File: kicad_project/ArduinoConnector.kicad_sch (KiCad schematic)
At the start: 12 parts, among them J5 1x8, J6 1x6, J7 1x10, J8 1x8

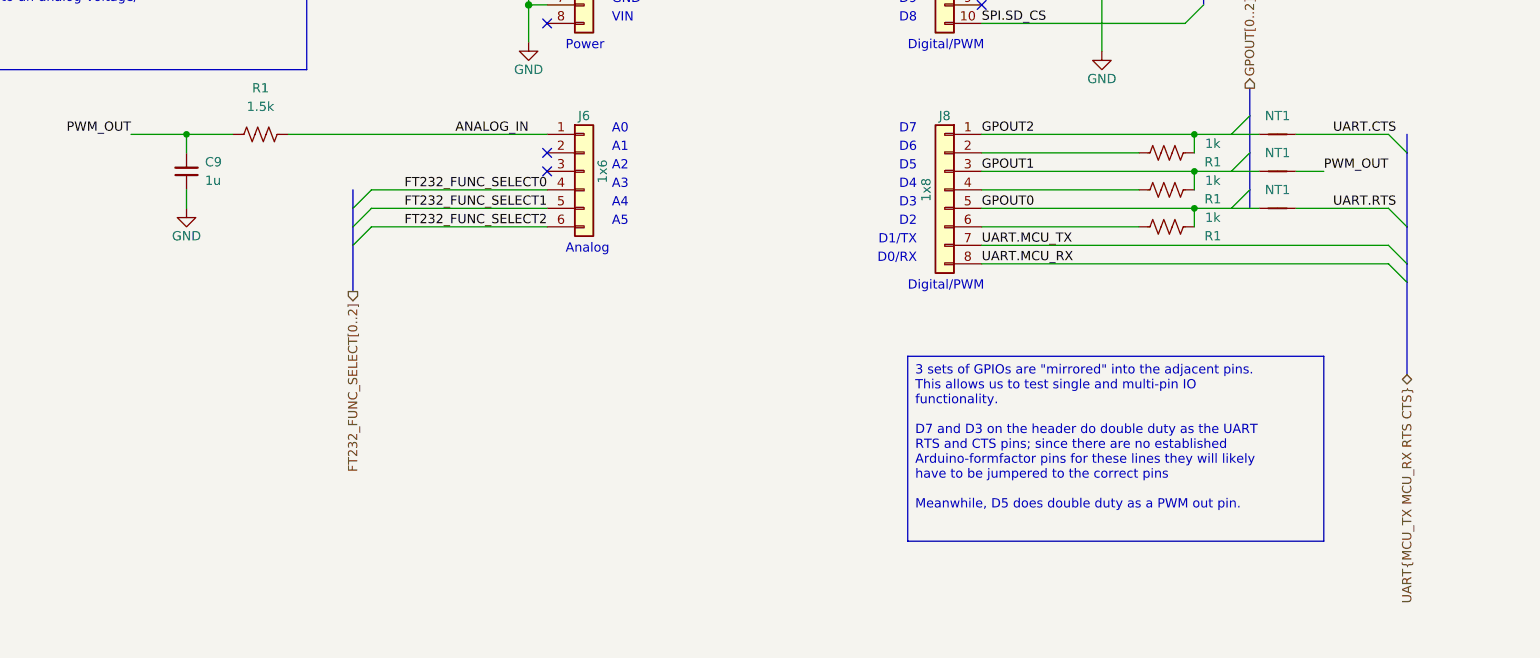
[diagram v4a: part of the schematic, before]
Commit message: Add diode on SD card CS line, fix position of PWM/analog testing capacitor
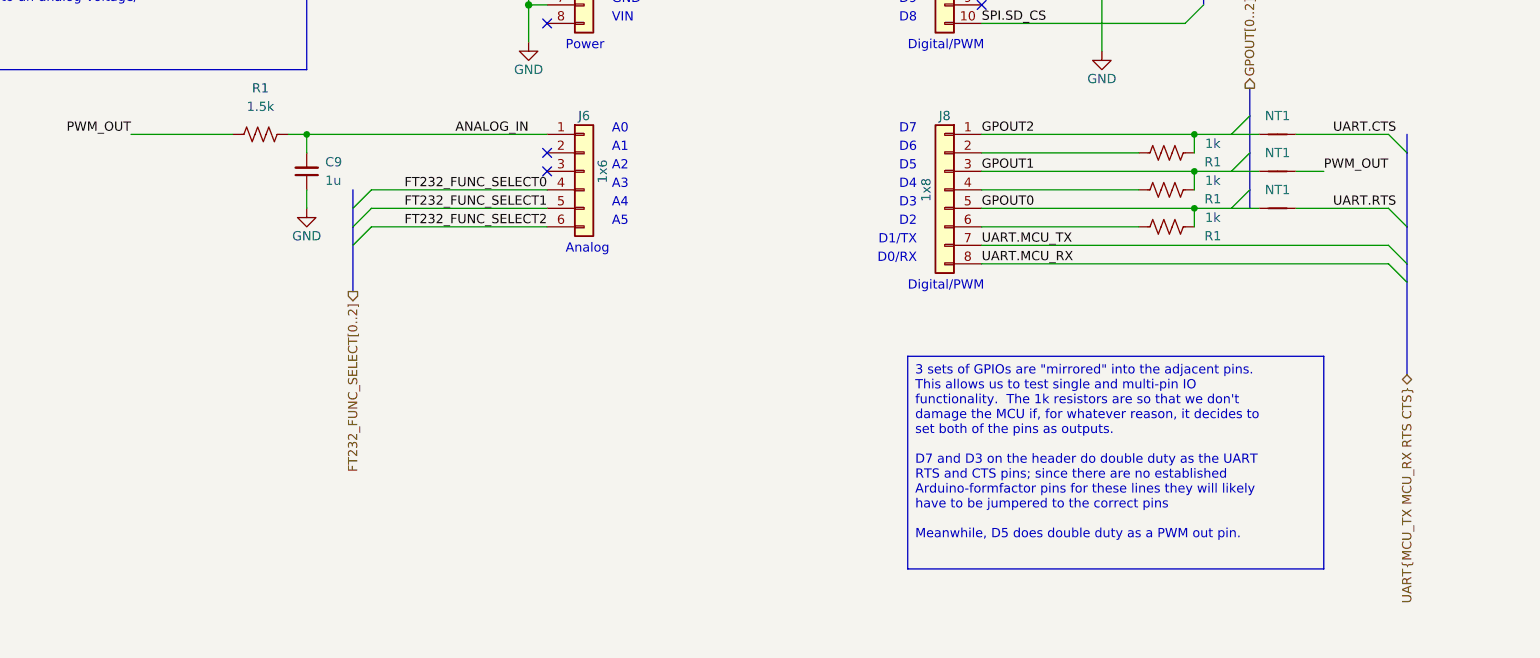
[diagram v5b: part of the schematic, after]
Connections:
- net ANALOG_IN: now also C9.2
- net PWM_OUT: no longer C9.2
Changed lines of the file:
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@@
   (junction (at 210.82 107.95) (diameter 0) (color 0 0 0 0)
   )
-  (junction (at 72.39 97.79) (diameter 0) (color 0 0 0 0)
-  )
   (junction (at 210.82 97.79) (diameter 0) (color 0 0 0 0)
+  )
+  (junction (at 88.9 97.79) (diameter 0) (color 0 0 0 0)
   )
   (junction (at 119.38 80.01) (diameter 1.016) (color 0 0 0 0)
@@
     (stroke (width 0) (type default))
   )
-  (wire (pts (xy 72.39 97.79) (xy 72.39 100.33))
-    (stroke (width 0) (type default))
-  )
   (bus (pts (xy 240.03 118.11) (xy 240.03 130.81))
     (stroke (width 0) (type default))
@@
     (stroke (width 0) (type default))
   )
+  (wire (pts (xy 88.9 105.41) (xy 88.9 107.95))
+    (stroke (width 0) (type default))
+  )
   (bus (pts (xy 95.25 105.41) (xy 95.25 107.95))
     (stroke (width 0) (type default))
@@
     (stroke (width 0) (type default))
   )
-  (wire (pts (xy 78.74 97.79) (xy 72.39 97.79))
+  (wire (pts (xy 64.77 97.79) (xy 78.74 97.79))
     (stroke (width 0) (type default))
   )
@@
   )
   (bus (pts (xy 212.09 74.93) (xy 212.09 80.01))
-    (stroke (width 0) (type default))
-  )
-  (wire (pts (xy 72.39 105.41) (xy 72.39 107.95))
-    (stroke (width 0) (type default))
-  )
-  (wire (pts (xy 64.77 97.79) (xy 72.39 97.79))
     (stroke (width 0) (type default))
   )
@@
     (stroke (width 0) (type default))
   )
+  (wire (pts (xy 88.9 97.79) (xy 88.9 100.33))
+    (stroke (width 0) (type default))
+  )
   (wire (pts (xy 119.38 80.01) (xy 119.38 85.09))
     (stroke (width 0) (type solid))
@@
     (stroke (width 0) (type default))
   )
-  (wire (pts (xy 86.36 97.79) (xy 121.92 97.79))
+  (wire (pts (xy 86.36 97.79) (xy 88.9 97.79))
     (stroke (width 0) (type default))
   )
@@
     (stroke (width 0) (type default))
   )
+  (wire (pts (xy 88.9 97.79) (xy 121.92 97.79))
+    (stroke (width 0) (type default))
+  )
   (wire (pts (xy 181.61 115.57) (xy 237.49 115.57))
     (stroke (width 0) (type default))
@@
     (effects (font (size 1.27 1.27)) (justify left top))
   )
-  (text_box "3 sets of GPIOs are \"mirrored\" into the adjacent pins.  This allows us to test single and multi-pin IO functionality.\n\nD7 and D3 on the header do double duty as the UART RTS and CTS pins; since there are no established Arduino-formfactor pins for these lines they will likely have to be jumpered to the correct pins\n\nMeanwhile, D5 does double duty as a PWM out pin."
-    (at 171.45 128.27 0) (size 57.15 25.4)
+  (text_box "3 sets of GPIOs are \"mirrored\" into the adjacent pins.  This allows us to test single and multi-pin IO functionality.  The 1k resistors are so that we don't damage the MCU if, for whatever reason, it decides to set both of the pins as outputs.\n\nD7 and D3 on the header do double duty as the UART RTS and CTS pins; since there are no established Arduino-formfactor pins for these lines they will likely have to be jumpered to the correct pins\n\nMeanwhile, D5 does double duty as a PWM out pin."
+    (at 171.45 128.27 0) (size 57.15 29.21)
     (stroke (width 0) (type default))
     (fill (type none))
@@
     )
   )
-  (symbol (lib_id "Device:C_Small") (at 72.39 102.87 180) (unit 1)
-    (in_bom yes) (on_board yes) (dnp no) (fields_autoplaced)
-    (property "Reference" "C9" (at 74.93 101.5936 0)
-      (effects (font (size 1.27 1.27)) (justify right))
-    )
-    (property "Value" "1u" (at 74.93 104.1336 0)
-      (effects (font (size 1.27 1.27)) (justify right))
-    )
-    (property "Footprint" "Capacitor_SMD:C_1206_3216Metric" (at 72.39 102.87 0)
-      (effects (font (size 1.27 1.27)) hide)
-    )
-    (property "Datasheet" "~" (at 72.39 102.87 0)
-      (effects (font (size 1.27 1.27)) hide)
-    )
-    (property "Supplier" "Digi-Key" (at 72.39 102.87 0)
-      (effects (font (size 1.27 1.27)) hide)
-    )
-    (property "LibRef" "CL31B105KBHNNNE" (at 72.39 102.87 0)
-      (effects (font (size 1.27 1.27)) hide)
-    )
-    (pin "1")
-    (pin "2")
-    (instances
-      (project "mbed-ce-ci-shield-v2"
-        (path "/a0f40274-9469-4bcf-885c-e8b8a490ea54/d2cb7c4f-a03f-4f1c-8cab-0427a0ad2909"
-          (reference "C9") (unit 1)
-        )
-        (path "/a0f40274-9469-4bcf-885c-e8b8a490ea54/1e471c6e-a872-4398-8c30-01f0a30d79ce"
-          (reference "C36") (unit 1)
-        )
-      )
-    )
-  )
   (symbol (lib_id "Device:R_US") (at 207.01 105.41 90) (unit 1)
     (in_bom yes) (on_board yes) (dnp no)
@@
         (path "/e63e39d7-6ac0-4ffd-8aa3-1841a4541b55"
           (reference "J1") (unit 1)
-        )
-      )
-    )
-  )
-  (symbol (lib_id "power:GND") (at 72.39 107.95 0) (unit 1)
-    (in_bom yes) (on_board yes) (dnp no)
-    (property "Reference" "#PWR066" (at 72.39 114.3 0)
-      (effects (font (size 1.27 1.27)) hide)
-    )
-    (property "Value" "GND" (at 72.39 111.76 0)
-      (effects (font (size 1.27 1.27)))
-    )
-    (property "Footprint" "" (at 72.39 107.95 0)
-      (effects (font (size 1.27 1.27)))
-    )
-    (property "Datasheet" "" (at 72.39 107.95 0)
-      (effects (font (size 1.27 1.27)))
-    )
-    (pin "1")
-    (instances
-      (project "mbed-ce-ci-shield-v2"
-        (path "/a0f40274-9469-4bcf-885c-e8b8a490ea54"
-          (reference "#PWR066") (unit 1)
-        )
-        (path "/a0f40274-9469-4bcf-885c-e8b8a490ea54/1e471c6e-a872-4398-8c30-01f0a30d79ce"
-          (reference "#PWR065") (unit 1)
-        )
-      )
-      (project "Arduino Uno Template"
-        (path "/e63e39d7-6ac0-4ffd-8aa3-1841a4541b55"
-          (reference "#PWR04") (unit 1)
         )
       )
@@
         )
       )
+    )
+  )
+  (symbol (lib_id "Device:C_Small") (at 88.9 102.87 180) (unit 1)
+    (in_bom yes) (on_board yes) (dnp no) (fields_autoplaced)
+    (property "Reference" "C9" (at 91.44 101.5936 0)
+      (effects (font (size 1.27 1.27)) (justify right))
+    )
+    (property "Value" "1u" (at 91.44 104.1336 0)
+      (effects (font (size 1.27 1.27)) (justify right))
+    )
+    (property "Footprint" "Capacitor_SMD:C_1206_3216Metric" (at 88.9 102.87 0)
+      (effects (font (size 1.27 1.27)) hide)
+    )
+    (property "Datasheet" "~" (at 88.9 102.87 0)
+      (effects (font (size 1.27 1.27)) hide)
+    )
+    (property "Supplier" "Digi-Key" (at 88.9 102.87 0)
+      (effects (font (size 1.27 1.27)) hide)
+    )
+    (property "LibRef" "CL31B105KBHNNNE" (at 88.9 102.87 0)
+      (effects (font (size 1.27 1.27)) hide)
+    )
+    (pin "1")
+    (pin "2")
+    (instances
+      (project "mbed-ce-ci-shield-v2"
+        (path "/a0f40274-9469-4bcf-885c-e8b8a490ea54/d2cb7c4f-a03f-4f1c-8cab-0427a0ad2909"
+          (reference "C9") (unit 1)
+        )
+        (path "/a0f40274-9469-4bcf-885c-e8b8a490ea54/1e471c6e-a872-4398-8c30-01f0a30d79ce"
+          (reference "C36") (unit 1)
+        )
+      )
+    )
+  )
+  (symbol (lib_id "power:GND") (at 88.9 107.95 0) (unit 1)
+    (in_bom yes) (on_board yes) (dnp no)
+    (property "Reference" "#PWR066" (at 88.9 114.3 0)
+      (effects (font (size 1.27 1.27)) hide)
+    )
+    (property "Value" "GND" (at 88.9 111.76 0)
+      (effects (font (size 1.27 1.27)))
+    )
+    (property "Footprint" "" (at 88.9 107.95 0)
+      (effects (font (size 1.27 1.27)))
+    )
+    (property "Datasheet" "" (at 88.9 107.95 0)
+      (effects (font (size 1.27 1.27)))
+    )
+    (pin "1")
+    (instances
+      (project "mbed-ce-ci-shield-v2"
+        (path "/a0f40274-9469-4bcf-885c-e8b8a490ea54"
+          (reference "#PWR066") (unit 1)
+        )
+        (path "/a0f40274-9469-4bcf-885c-e8b8a490ea54/1e471c6e-a872-4398-8c30-01f0a30d79ce"
+          (reference "#PWR065") (unit 1)
+        )
+      )
+      (project "Arduino Uno Template"
+        (path "/e63e39d7-6ac0-4ffd-8aa3-1841a4541b55"
+          (reference "#PWR04") (unit 1)
+        )
+      )

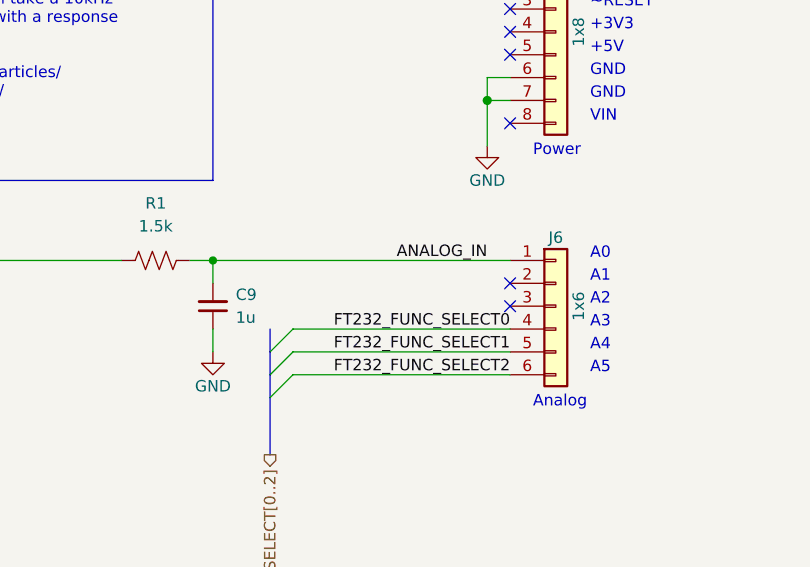
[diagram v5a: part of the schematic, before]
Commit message: Update MicroSD card socket to have analog switch
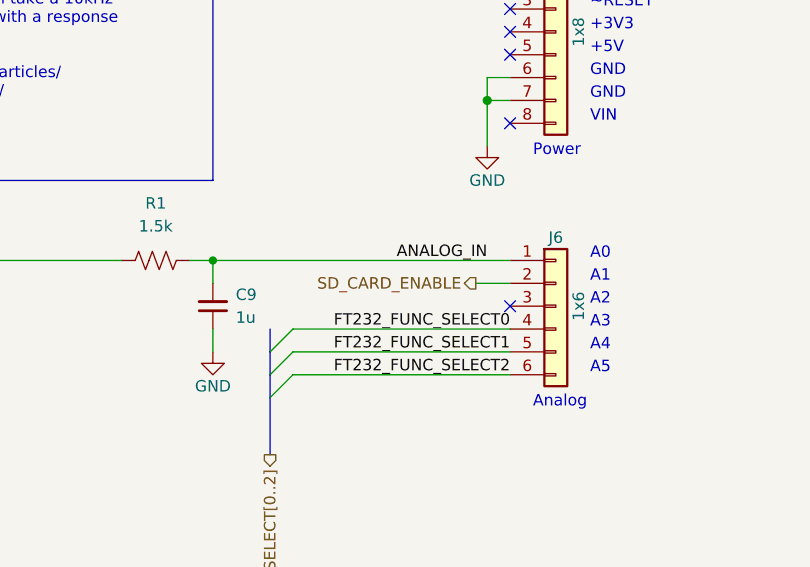
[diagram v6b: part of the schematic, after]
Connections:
- net SD_CARD_ENABLE: now reaches J6.2 (Pin_2)
- no-connect marks 10 -> 9
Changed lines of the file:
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@@
   (no_connect (at 121.92 102.87))
   (no_connect (at 181.61 80.01))
-  (no_connect (at 121.92 100.33))
   (no_connect (at 121.92 67.31))
   (no_connect (at 121.92 82.55))
@@
     (stroke (width 0) (type default))
   )
+  (wire (pts (xy 118.11 100.33) (xy 121.92 100.33))
+    (stroke (width 0) (type default))
+  )
   (bus (pts (xy 240.03 100.33) (xy 240.03 110.49))
     (stroke (width 0) (type default))
@@
     (effects (font (size 1.27 1.27)) (justify right))
   )
+  (hierarchical_label "SD_CARD_ENABLE" (shape output) (at 118.11 100.33 180) (fields_autoplaced)
+    (effects (font (size 1.27 1.27)) (justify right))
+  )

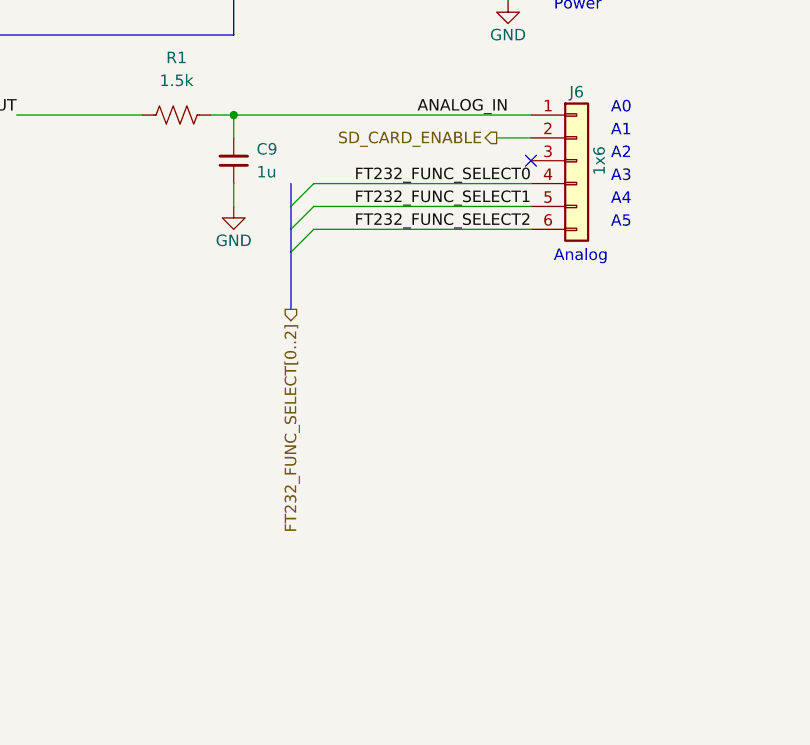
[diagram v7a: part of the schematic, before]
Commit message: Finish Rev 2 schematic, start on routing
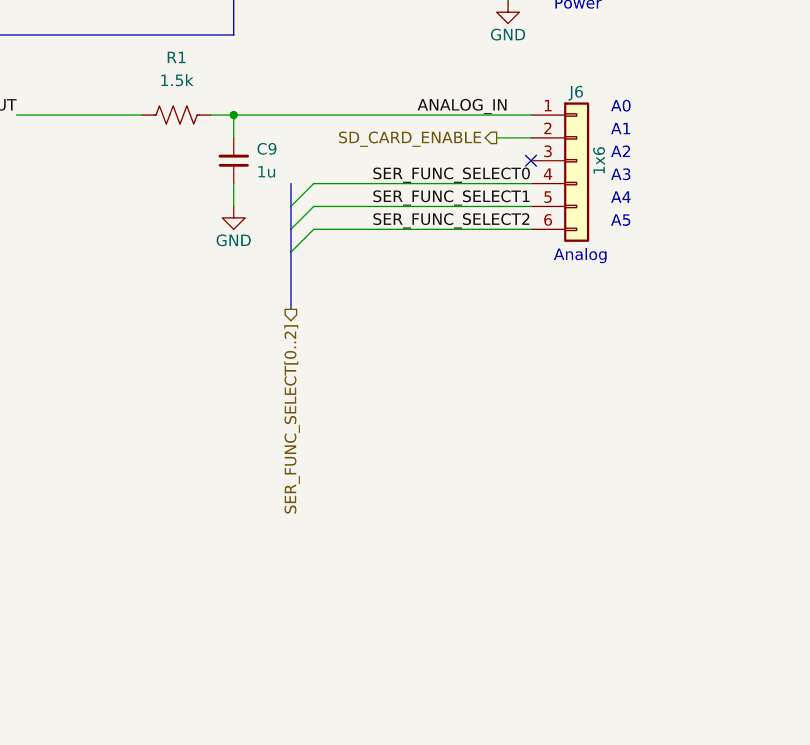
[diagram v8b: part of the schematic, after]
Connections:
- net FT232_FUNC_SELECT0 renamed SER_FUNC_SELECT0
- net FT232_FUNC_SELECT1 renamed SER_FUNC_SELECT1
- net FT232_FUNC_SELECT2 renamed SER_FUNC_SELECT2
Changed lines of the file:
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@@
     (effects (font (size 1.27 1.27)) (justify left bottom))
   )
-  (label "FT232_FUNC_SELECT1" (at 121.92 107.95 180) (fields_autoplaced)
+  (label "SER_FUNC_SELECT1" (at 121.92 107.95 180) (fields_autoplaced)
     (effects (font (size 1.27 1.27)) (justify right bottom))
   )
@@
     (effects (font (size 1.27 1.27)) (justify left bottom))
   )
-  (label "FT232_FUNC_SELECT0" (at 121.92 105.41 180) (fields_autoplaced)
+  (label "SER_FUNC_SELECT0" (at 121.92 105.41 180) (fields_autoplaced)
     (effects (font (size 1.27 1.27)) (justify right bottom))
   )
-  (label "FT232_FUNC_SELECT2" (at 121.92 110.49 180) (fields_autoplaced)
+  (label "SER_FUNC_SELECT2" (at 121.92 110.49 180) (fields_autoplaced)
     (effects (font (size 1.27 1.27)) (justify right bottom))
   )
@@
     (effects (font (size 1.27 1.27)) (justify left))
   )
-  (hierarchical_label "FT232_FUNC_SELECT[0..2]" (shape output) (at 95.25 119.38 270) (fields_autoplaced)
+  (hierarchical_label "SER_FUNC_SELECT[0..2]" (shape output) (at 95.25 119.38 270) (fields_autoplaced)
     (effects (font (size 1.27 1.27)) (justify right))
   )
